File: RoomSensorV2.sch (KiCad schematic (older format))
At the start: 15 parts, among them J1 Conn_01x02, Q1 TP0606N3-G, U1 DS3231SN#, U2 ChipCap2-SIP, U3 SeeeduinoXIAO

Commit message: added PCB
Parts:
- U1: footprint Package_SO:SOIC-16W_7.5x10.3mm_P1.27mm -> SOIC127P1032X265-16N
- renumbered MODULE1 to U4
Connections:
- net GND: now also U1.10 (NC), U1.11 (NC), U1.12 (NC), U1.5 (NC), U1.6 (NC), U1.7 (NC), U1.8 (NC), U1.9 (NC)
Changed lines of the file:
@@
 $EndComp
 $Comp
-L RoomSensorV2:RN2483-I_RM095 MODULE1
+L RoomSensorV2:RN2483-I_RM095 U4
 U 1 1 604443EF
 P 8250 2500
-F 0 "MODULE1" H 8250 3967 50  0000 C CNN
+F 0 "U4" H 8250 3967 50  0000 C CNN
 F 1 "RN2483-I_RM095" H 8250 3876 50  0000 C CNN
 F 2 "RoomSensorV2:RM095" H 8250 2500 50  0001 L BNN
@@
 L power:GND #PWR0101
 U 1 1 6044EE3E
-P 2400 3450
-F 0 "#PWR0101" H 2400 3200 50  0001 C CNN
-F 1 "GND" H 2405 3277 50  0000 C CNN
-F 2 "" H 2400 3450 50  0001 C CNN
-F 3 "" H 2400 3450 50  0001 C CNN
-	1    2400 3450
+P 2150 3700
+F 0 "#PWR0101" H 2150 3450 50  0001 C CNN
+F 1 "GND" H 2155 3527 50  0000 C CNN
+F 2 "" H 2150 3700 50  0001 C CNN
+F 3 "" H 2150 3700 50  0001 C CNN
+	1    2150 3700
 	1    0    0    -1
 $EndComp
@@
 	1    0    0    -1
 $EndComp
-Wire Wire Line
-	2400 3450 2400 3400
 Text GLabel 7500 4300 0    50   Input ~ 0
 UART_TX
@@
 $Comp
 L RoomSensorV2:DS3231SN# U1
-U 1 1 6064706B
+U 1 1 60617FBF
 P 1750 3100
 F 0 "U1" H 1750 3667 50  0000 C CNN
 F 1 "DS3231SN#" H 1750 3576 50  0000 C CNN
-F 2 "Package_SO:SOIC-16W_7.5x10.3mm_P1.27mm" H 1750 3100 50  0001 L BNN
+F 2 "SOIC127P1032X265-16N" H 1750 3100 50  0001 L BNN
 F 3 "https://no.mouser.com/datasheet/2/256/DS3231-1513891.pdf" H 1750 3100 50  0001 L BNN
 F 4 "Maxim Intergrated" H 1750 3100 50  0001 L BNN "MANUFACTURER"
@@
 	1    0    0    -1
 $EndComp
+Wire Wire Line
+	1500 3600 1500 3650
+Wire Wire Line
+	1500 3650 1550 3650
+Wire Wire Line
+	2400 3400 2400 3650
+Wire Wire Line
+	2150 3700 2150 3650
+Connection ~ 2150 3650
+Wire Wire Line
+	2150 3650 2400 3650
+Wire Wire Line
+	1850 3650 1850 3600
+Connection ~ 1850 3650
+Wire Wire Line
+	1850 3650 2150 3650
+Wire Wire Line
+	1800 3600 1800 3650
+Connection ~ 1800 3650
+Wire Wire Line
+	1800 3650 1850 3650
+Wire Wire Line
+	1750 3650 1750 3600
+Connection ~ 1750 3650
+Wire Wire Line
+	1750 3650 1800 3650
+Wire Wire Line
+	1700 3600 1700 3650
+Connection ~ 1700 3650
+Wire Wire Line
+	1700 3650 1750 3650
+Wire Wire Line
+	1650 3650 1650 3600
+Connection ~ 1650 3650
+Wire Wire Line
+	1650 3650 1700 3650
+Wire Wire Line
+	1600 3600 1600 3650
+Connection ~ 1600 3650
+Wire Wire Line
+	1600 3650 1650 3650
+Wire Wire Line
+	1550 3650 1550 3600
+Connection ~ 1550 3650
+Wire Wire Line
+	1550 3650 1600 3650
 $EndSCHEMATC

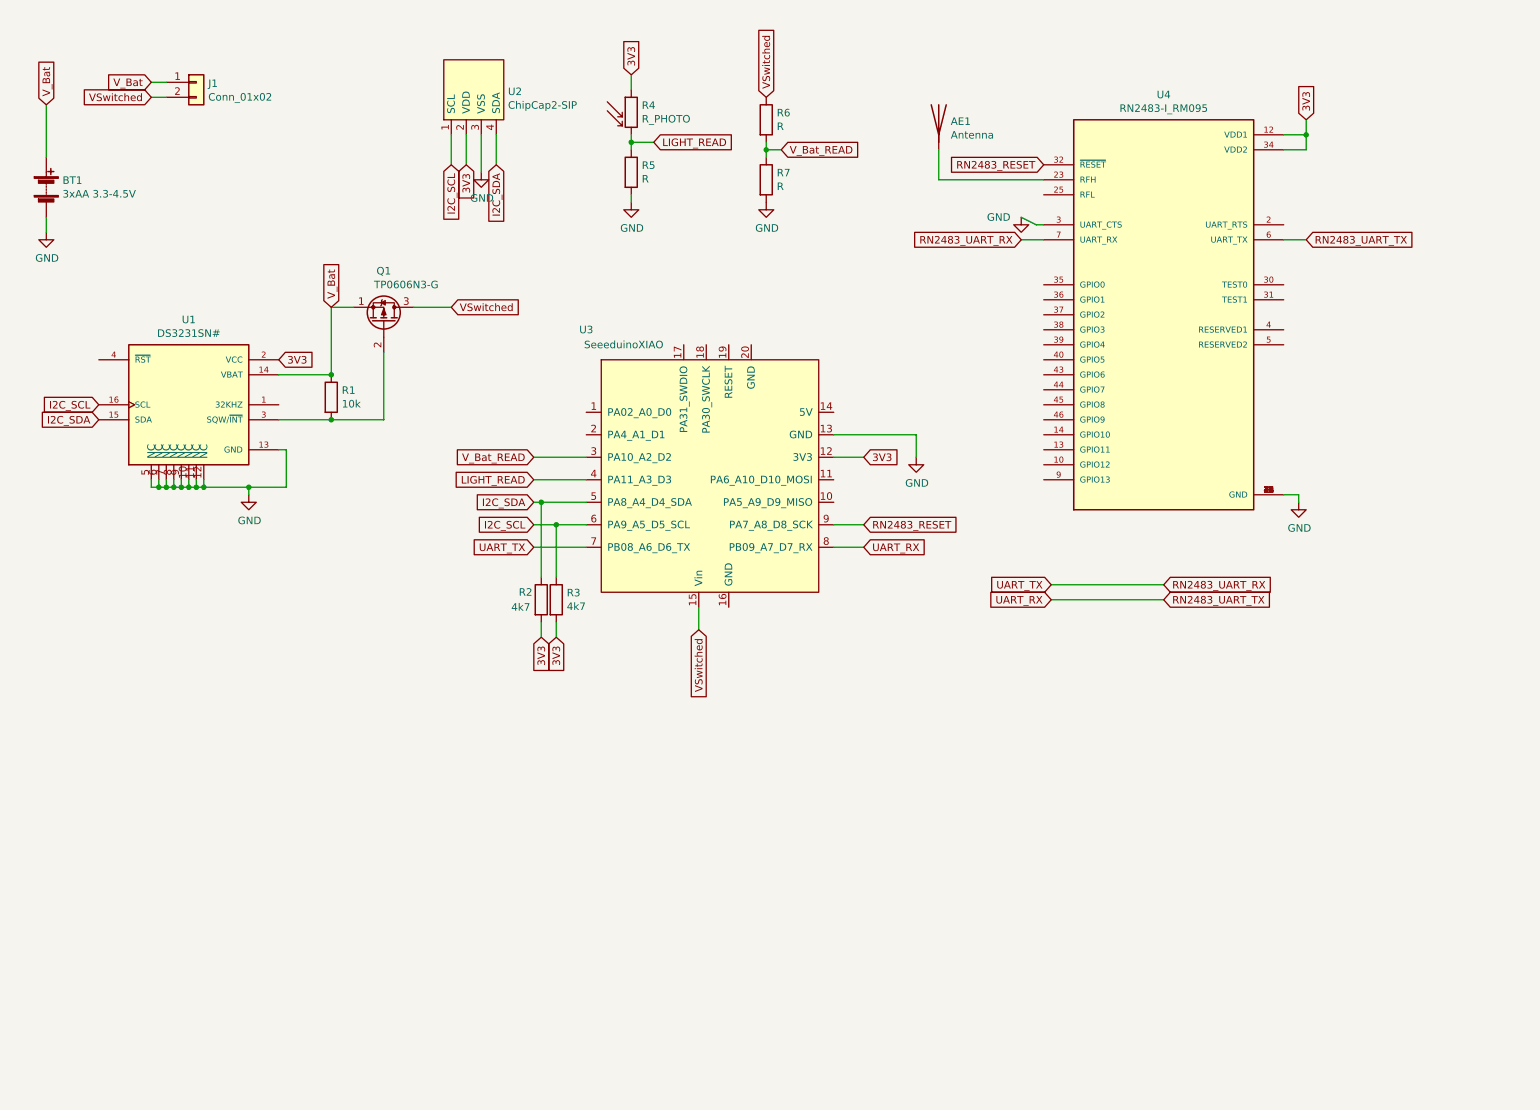
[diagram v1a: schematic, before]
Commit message: Replaced Seeeduino XIAO by using ATSAMD21G18A microcontroller directly
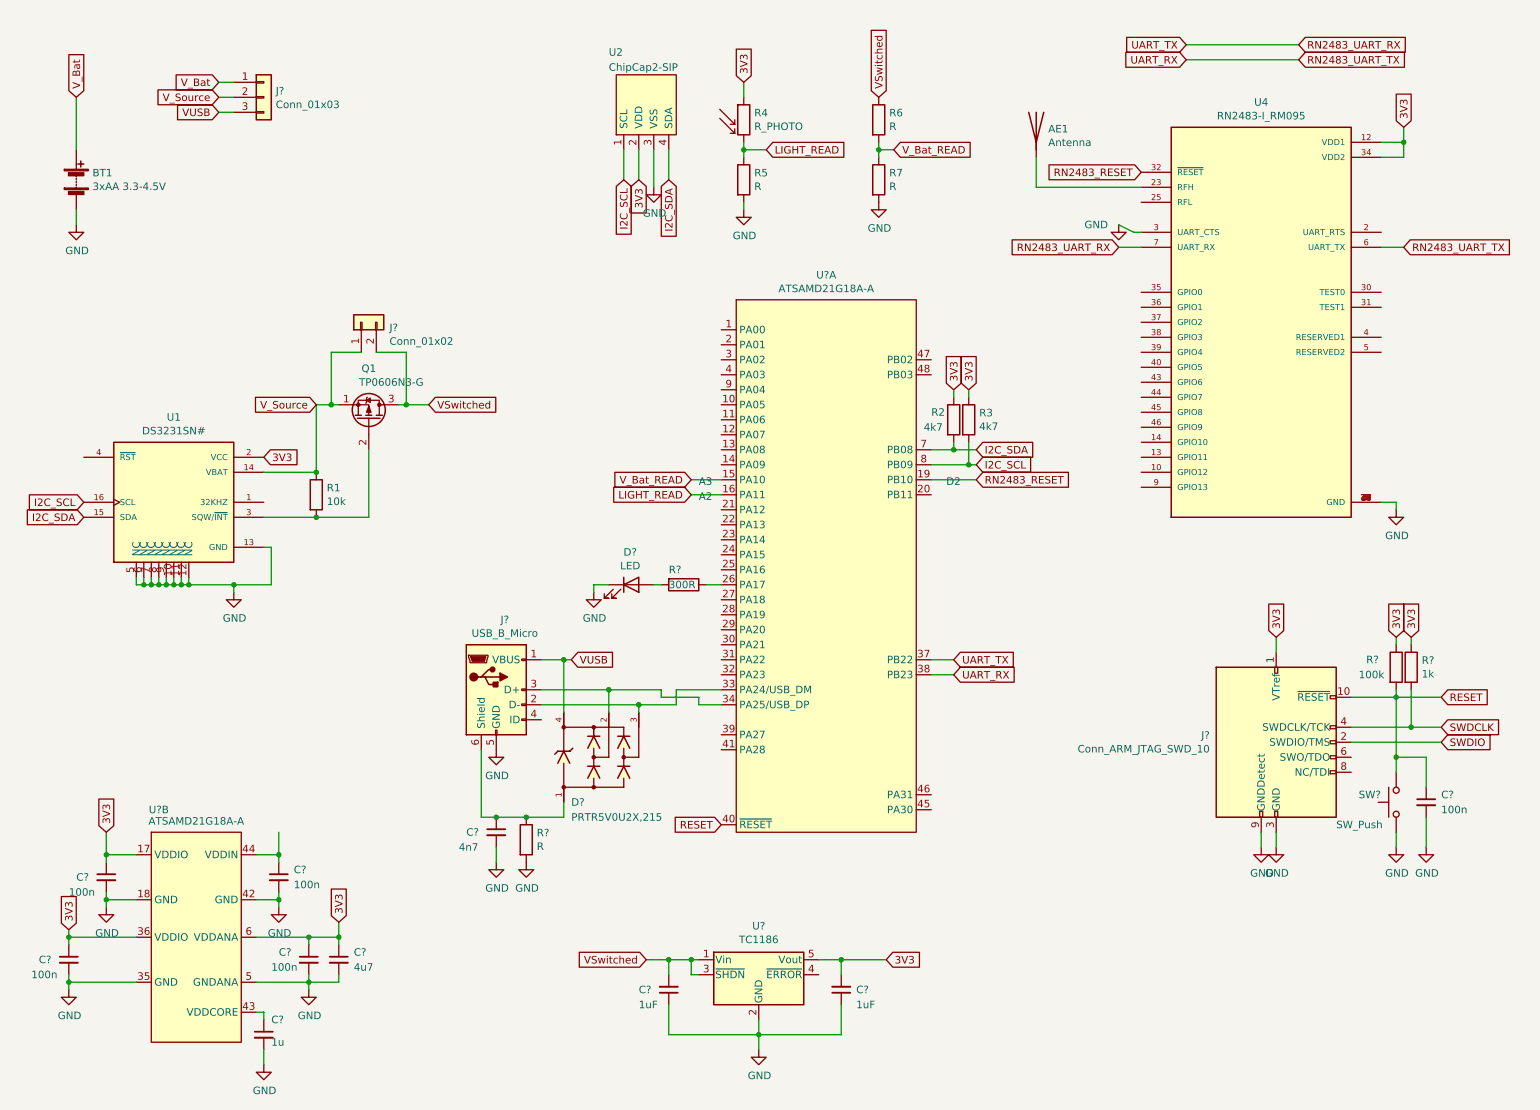
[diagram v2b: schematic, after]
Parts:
- removed J1: Conn_01x02, Connector_PinHeader_2.54mm:PinHeader_1x02_P2.54mm_Vertical, symbol Connector_Generic:Conn_01x02
- removed U3: SeeeduinoXIAO, RoomSensorV2:SeeeduinoXIAO_SMD, symbol RoomSensorV2:SeeeduinoXIAO
- added C?: 4n7, symbol Device:C_Small
- added C? (x2): 1uF, symbol Device:C_Small
- added C? (x5): 100n, symbol Device:C_Small
- added C?: 4u7, symbol Device:C_Small
- added C?: 1u, symbol Device:C_Small
- added D?: PRTR5V0U2X,215, SOT143B, symbol RoomSensorV2:PRTR5V0U2X,215
- added D?: LED, symbol Device:LED
- added J?: USB_B_Micro, symbol Connector:USB_B_Micro
- added J?: Conn_01x03, symbol Connector_Generic:Conn_01x03
- added J?: Conn_01x02, symbol Connector_Generic:Conn_01x02
- added J?: Conn_ARM_JTAG_SWD_10, symbol Connector:Conn_ARM_JTAG_SWD_10
- added R?: R, symbol Device:R
- added R?: 1k, symbol Device:R
- added R?: 100k, symbol Device:R
- added R?: 300R, Resistor_THT:R_Axial_DIN0207_L6.3mm_D2.5mm_P10.16mm_Horizontal, symbol Device:R
- added SW?: SW_Push, symbol Switch:SW_Push
- added U?: TC1186, Package_TO_SOT_SMD:SOT-23-5, symbol Regulator_Linear:TC1186
- added U? (x2): ATSAMD21G18A-A, Package_QFP:TQFP-48_7x7mm_P0.5mm, symbol RoomSensorV2:ATSAMD21G18A-A
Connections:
- net 3V3: now also R2.1, R3.1, C?.1, C?.1, C?.1, C?.1, C?.2, J?.1 (VTref), R?.1, R?.1, U?.17 (VDDIO), U?.36 (VDDIO), U?.5 (Vout), U?.6 (VDDANA); no longer R2.2, R3.2
- net GND: now also C?.1, C?.1, C?.2, C?.2, C?.2, C?.2, C?.2, C?.2, C?.2, C?.2, D?.1 (K), J?.3 (GND), J?.5 (GND), J?.5 (GND), J?.9 (GNDDetect), R?.2, SW?.1, U?.18 (GND), U?.2 (GND), U?.35 (GND), U?.42 (GND), U?.5 (GNDANA)
- net I2C_SCL: now also R3.2, U?.8 (PB09); no longer R3.1
- net I2C_SDA: now also R2.2, U?.7 (PB08); no longer R2.1
- net LIGHT_READ: now also U?.16 (PA11)
- net RN2483_RESET: now also U?.19 (PB10)
- net RN2483_UART_RX: now also U?.37 (PB22)
- net RN2483_UART_TX: now also U?.38 (PB23)
- net VSwitched: now also C?.2, J?.2 (Pin_2), U?.1 (Vin), U?.3 (~SHDN)
- net V_Bat: now also J?.1 (Pin_1); no longer Q1.1 (S), R1.1, U1.14 (VBAT)
- net V_Bat_READ: now also U?.15 (PA10)
- new net: D?.3, J?.2 (D-), U?.33 (PA24/USB_DM)
- new net: D?.2, J?.3 (D+), U?.34 (PA25/USB_DP)
- new net: C?.1, D?.1, J?.6 (Shield), R?.1
- new net: R?.1, U?.26 (PA17)
- new net: C?.1, U?.43 (VDDCORE)
- new net: C?.1, U?.44 (VDDIN)
- new net: D?.2 (A), R?.2
- new net RESET: C?.1, J?.10 (~RESET~), R?.2, SW?.2, U?.40 (~RESET)
- new net SWDCLK: J?.4 (SWDCLK/TCK), R?.2
- new net SWDIO: J?.2 (SWDIO/TMS)
- new net VUSB: D?.4, J?.1 (VBUS), J?.3 (Pin_3)
- new net V_Source: J?.1 (Pin_1), J?.2 (Pin_2), Q1.1 (S), R1.1, U1.14 (VBAT)
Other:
- note added: "A2"
- note added: "A3"
- note added: "D2"
- moved on the sheet: AE1, BT1, Q1, R1, R2, R3, R4, R5, R6, R7, U1, U2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

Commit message: Revision 1.0
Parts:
- removed J?: USB_B_Micro, symbol Connector:USB_B_Micro
- removed SW?: SW_Push, symbol Switch:SW_Push
- added C10: 1uF, Capacitor_SMD:C_0805_2012Metric, symbol Device:C_Small
- added J3: DX07S016JA1R1500, RoomSensorV2:JAE_DX07S016JA1R1500, symbol RoomSensorV2:DX07S016JA1R1500
- added R13, R8: 5k1, Resistor_SMD:R_0805_2012Metric, symbol Device:R
- added TP1: TestPoint_2Pole, Jumper:SolderJumper-2_P1.3mm_Open_RoundedPad1.0x1.5mm, symbol Connector:TestPoint_2Pole
- C1, C11, C2, C4, C5, C6, C7: renamed from C?; footprint (none) -> Capacitor_SMD:C_0805_2012Metric
- C3: renamed from C?; value 1u -> 1uF; footprint (none) -> Capacitor_SMD:C_0805_2012Metric
- C8, C9: renamed from C?; value 1uF -> 10uF; footprint (none) -> Capacitor_SMD:C_0805_2012Metric
- D1: renamed from D?; value LED -> LED BLUE APTD2012LQBC/D; footprint (none) -> LED_SMD:LED_0805_2012Metric
- D2: renamed from D?; footprint SOT143B -> RoomSensorV2:SOT143B
- J1: renamed from J?; footprint (none) -> Connector_PinHeader_2.54mm:PinHeader_1x03_P2.54mm_Vertical
- J2: renamed from J?; footprint (none) -> Connector_PinHeader_2.54mm:PinHeader_1x02_P2.54mm_Vertical
- J4: renamed from J?; value Conn_ARM_JTAG_SWD_10 -> SHF-105-01-F-D-SM; footprint (none) -> RoomSensorV2:SHF-105-01-X-D-SM
- R1, R2, R3: footprint Resistor_THT:R_Axial_DIN0207_L6.3mm_D2.5mm_P10.16mm_Horizontal -> Resistor_SMD:R_0805_2012Metric
- R10: renamed from R?; footprint Resistor_THT:R_Axial_DIN0207_L6.3mm_D2.5mm_P10.16mm_Horizontal -> Resistor_SMD:R_0805_2012Metric
- R11, R12: renamed from R?; footprint (none) -> Resistor_SMD:R_0805_2012Metric
- R5: value R -> 10k / 100k; footprint Resistor_THT:R_Axial_DIN0207_L6.3mm_D2.5mm_P10.16mm_Horizontal -> Resistor_SMD:R_0805_2012Metric
- R6, R7: value R -> 10k; footprint Resistor_THT:R_Axial_DIN0207_L6.3mm_D2.5mm_P10.16mm_Horizontal -> Resistor_SMD:R_0805_2012Metric
- R9: renamed from R?; value R -> 1M; footprint (none) -> Resistor_SMD:R_0805_2012Metric
- U1: footprint SOIC127P1032X265-16N -> Package_SO:SOIC-16W_7.5x10.3mm_P1.27mm
- gave numbers to parts that had none: 2
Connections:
- net 3V3: now also U3.17 (VDDIO), U3.36 (VDDIO), U3.6 (VDDANA), C10.2; no longer U3.17 (VDDIO), U3.36 (VDDIO), U3.6 (VDDANA)
- net GND: now also U3.18 (GND), U3.35 (GND), U3.42 (GND), U3.5 (GNDANA), C10.1, J3.1 (GND), J3.12 (GND), R13.1, R8.2, TP1.2; no longer U3.18 (GND), U3.35 (GND), U3.42 (GND), U3.5 (GNDANA)
- net I2C_SCL: now also U3.8 (PB09); no longer U3.8 (PB09)
- net I2C_SDA: now also U3.7 (PB08); no longer U3.7 (PB08)
- net LIGHT_READ: now also U3.16 (PA11); no longer U3.16 (PA11)
- net RESET: now also U3.40 (~RESET), TP1.1; no longer U3.40 (~RESET)
- net RN2483_RESET: now also U3.19 (PB10); no longer U3.19 (PB10)
- net RN2483_UART_RX: now also U3.37 (PB22); no longer U3.37 (PB22)
- net RN2483_UART_TX: now also U3.38 (PB23); no longer U3.38 (PB23)
- net SWDCLK: now also U3.45 (PA30)
- net SWDIO: now also U3.46 (PA31)
- net VUSB: now also J3.11 (VBUS), J3.2 (VBUS)
- net V_Bat_READ: now also U3.15 (PA10); no longer U3.15 (PA10)
- net at D2.3: now also U3.33 (PA24/USB_DM), J3.5 (D-), J3.8 (D-); no longer U3.33 (PA24/USB_DM)
- net at D2.2: now also U3.34 (PA25/USB_DP), J3.6 (D+), J3.7 (D+); no longer U3.34 (PA25/USB_DP)
- net at C7.1, D2.1, R9.1: now also J3.S1 (SHIELD), J3.S2 (SHIELD), J3.S3 (SHIELD), J3.S4 (SHIELD), J3.S5 (SHIELD), J3.S6 (SHIELD)
- net at R10.1: now also U3.26 (PA17); no longer U3.26 (PA17)
- net at C3.1: now also U3.43 (VDDCORE); no longer U3.43 (VDDCORE)
- net at C4.1: now also U3.44 (VDDIN); no longer U3.44 (VDDIN)
- new net: J3.3 (CC1), R13.2
- new net: J3.9 (CC2), R8.1
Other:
- moved on the sheet: C7, D2, R9
